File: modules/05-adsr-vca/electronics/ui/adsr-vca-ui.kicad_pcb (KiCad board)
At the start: 2 copper layers, 58 x 110 mm, 40 parts, among them J1 Conn_02x03_Odd_Even, J3 Conn_02x03_Odd_Even, J4 Conn_01x02, J5 Conn_01x06, J6 Conn_02x03_Odd_Even, J8 Conn_02x03_Odd_Even, Q1 2N3904, Q2 2N3906

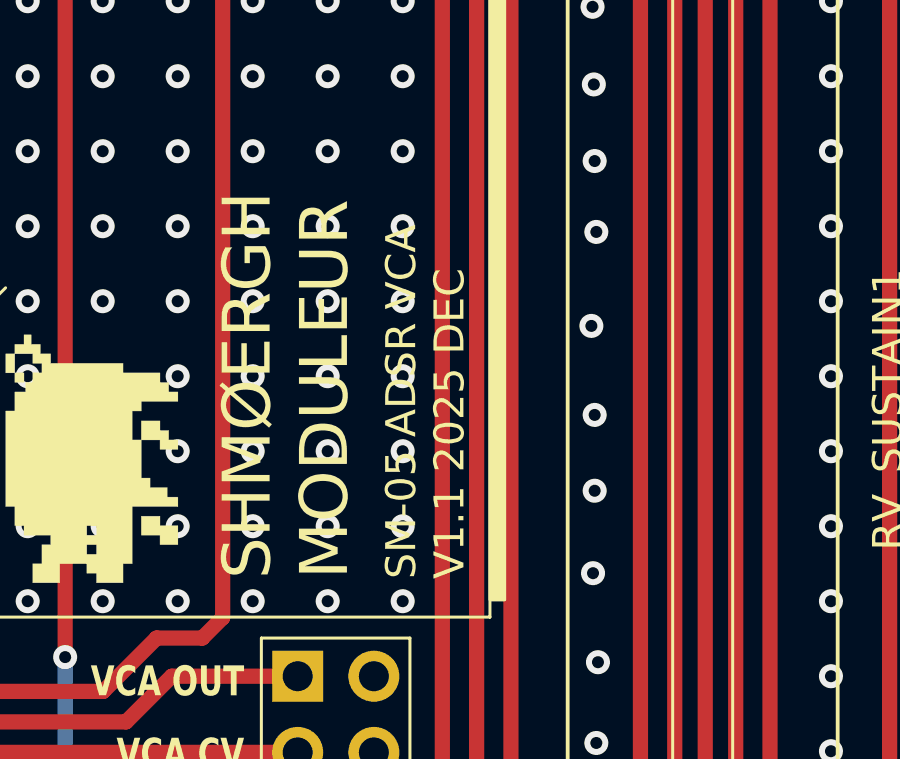
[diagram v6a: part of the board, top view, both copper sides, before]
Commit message: KiCAD version update - ADSR+VCA
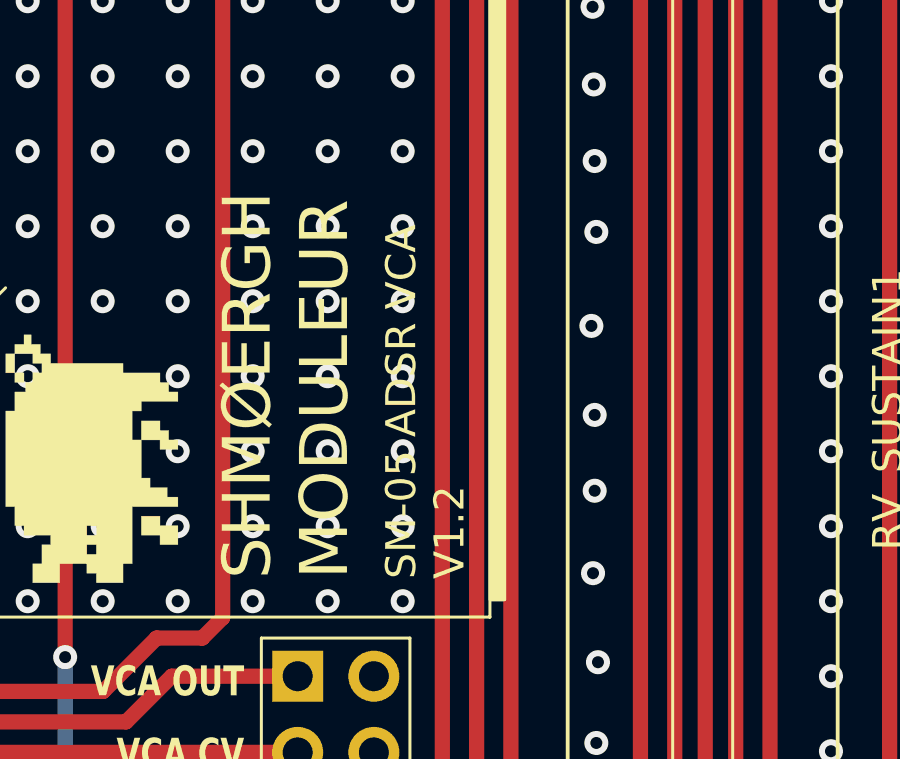
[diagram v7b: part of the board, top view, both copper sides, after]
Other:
- board text added: "SM-05 ADSR VCA V1.2"
- board text removed: "SM-05 ADSR VCA V1.1 2025 DEC"
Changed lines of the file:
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@@
 		)
 	)
-	(gr_text "SM-05 ADSR VCA\nV1.1 2025 DEC"
+	(gr_text "SM-05 ADSR VCA\nV1.2"
 		(at 161.1475 88.2595 90)
 		(layer "F.SilkS")
@@
 			(justify left bottom)
 		)
-		(render_cache "SM-05 ADSR VCA\nV1.1 2025 DEC" 90
+		(render_cache "SM-05 ADSR VCA\nV1.2" 90
 			(polygon
 				(pts
@@
 			(polygon
 				(pts
-					(xy 160.213874 85.207624) (xy 160.850249 85.207624) (xy 160.850249 85.462186) (xy 160.9775 85.462186)
-					(xy 160.9775 84.825811) (xy 160.850249 84.825811) (xy 160.850249 85.080374) (xy 159.959312 85.080374)
-					(xy 159.959312 85.207624) (xy 160.086624 85.207624) (xy 160.086624 85.462186) (xy 160.213874 85.462186)
-				)
-			)
-			(polygon
-				(pts
-					(xy 160.722998 83.682144) (xy 160.9775 83.682144) (xy 160.9775 83.04577) (xy 160.850249 83.04577)
-					(xy 160.850249 83.554894) (xy 160.722998 83.554894)
-				)
-			)
-			(polygon
-				(pts
-					(xy 160.086624 83.173081) (xy 159.959312 83.173081) (xy 159.959312 83.554894) (xy 160.086624 83.554894)
-				)
-			)
-			(polygon
-				(pts
-					(xy 160.086624 83.173081) (xy 160.341186 83.173081) (xy 160.341186 83.04577) (xy 160.086624 83.04577)
-				)
-			)
-			(polygon
-				(pts
-					(xy 160.595687 83.554894) (xy 160.722998 83.554894) (xy 160.722998 83.427582) (xy 160.595687 83.427582)
-				)
-			)
-			(polygon
-				(pts
-					(xy 160.086624 83.682144) (xy 160.213874 83.682144) (xy 160.213874 83.554894) (xy 160.086624 83.554894)
-				)
-			)
-			(polygon
-				(pts
-					(xy 160.341186 83.300332) (xy 160.468436 83.300332) (xy 160.468436 83.173081) (xy 160.341186 83.173081)
-				)
-			)
-			(polygon
-				(pts
-					(xy 160.468436 83.427582) (xy 160.595687 83.427582) (xy 160.595687 83.300332) (xy 160.468436 83.300332)
-				)
-			)
-			(polygon
-				(pts
-					(xy 160.086624 82.792123) (xy 160.850249 82.792123) (xy 160.850249 82.664873) (xy 160.595687 82.664873)
-					(xy 160.595687 82.537561) (xy 160.468436 82.537561) (xy 160.468436 82.664873) (xy 160.086624 82.664873)
-				)
-			)
-			(polygon
-				(pts
-					(xy 160.850249 82.664873) (xy 160.9775 82.664873) (xy 160.9775 82.28306) (xy 160.850249 82.28306)
-				)
-			)
-			(polygon
-				(pts
-					(xy 159.959312 82.664873) (xy 160.086624 82.664873) (xy 160.086624 82.28306) (xy 159.959312 82.28306)
-				)
-			)
-			(polygon
-				(pts
-					(xy 160.086624 82.28306) (xy 160.213874 82.28306) (xy 160.213874 82.410311) (xy 160.341186 82.410311)
-					(xy 160.341186 82.28306) (xy 160.850249 82.28306) (xy 160.850249 82.155749) (xy 160.086624 82.155749)
-				)
-			)
-			(polygon
-				(pts
-					(xy 160.341186 82.537561) (xy 160.468436 82.537561) (xy 160.468436 82.410311) (xy 160.341186 82.410311)
-				)
-			)
-			(polygon
-				(pts
-					(xy 160.722998 81.902102) (xy 160.9775 81.902102) (xy 160.9775 81.265728) (xy 160.850249 81.265728)
-					(xy 160.850249 81.774852) (xy 160.722998 81.774852)
-				)
-			)
-			(polygon
-				(pts
-					(xy 160.086624 81.393039) (xy 159.959312 81.393039) (xy 159.959312 81.774852) (xy 160.086624 81.774852)
-				)
-			)
-			(polygon
-				(pts
-					(xy 160.086624 81.393039) (xy 160.341186 81.393039) (xy 160.341186 81.265728) (xy 160.086624 81.265728)
-				)
-			)
-			(polygon
-				(pts
-					(xy 160.595687 81.774852) (xy 160.722998 81.774852) (xy 160.722998 81.64754) (xy 160.595687 81.64754)
-				)
-			)
-			(polygon
-				(pts
-					(xy 160.086624 81.902102) (xy 160.213874 81.902102) (xy 160.213874 81.774852) (xy 160.086624 81.774852)
-				)
-			)
-			(polygon
-				(pts
-					(xy 160.341186 81.52029) (xy 160.468436 81.52029) (xy 160.468436 81.393039) (xy 160.341186 81.393039)
-				)
-			)
-			(polygon
-				(pts
-					(xy 160.468436 81.64754) (xy 160.595687 81.64754) (xy 160.595687 81.52029) (xy 160.468436 81.52029)
-				)
-			)
-			(polygon
-				(pts
-					(xy 159.959312 81.012081) (xy 160.468436 81.012081) (xy 160.468436 80.503018) (xy 160.341186 80.503018)
-					(xy 160.341186 80.884831) (xy 160.086624 80.884831) (xy 160.086624 80.375707) (xy 159.959312 80.375707)
-				)
-			)
-			(polygon
-				(pts
-					(xy 160.468436 80.503018) (xy 160.850249 80.503018) (xy 160.850249 80.375707) (xy 160.468436 80.375707)
-				)
-			)
-			(polygon
-				(pts
-					(xy 160.850249 80.503018) (xy 160.850249 80.884831) (xy 160.9775 80.884831) (xy 160.9775 80.503018)
-				)
-			)
-			(polygon
-				(pts
-					(xy 160.850249 80.884831) (xy 160.722998 80.884831) (xy 160.722998 81.012081) (xy 160.850249 81.012081)
-				)
-			)
-			(polygon
-				(pts
-					(xy 159.959312 79.23204) (xy 160.9775 79.23204) (xy 160.9775 78.722976) (xy 160.850249 78.722976)
-					(xy 160.850249 79.104789) (xy 160.086624 79.104789) (xy 160.086624 78.722976) (xy 159.959312 78.722976)
-				)
-			)
-			(polygon
-				(pts
-					(xy 160.086624 78.722976) (xy 160.850249 78.722976) (xy 160.850249 78.595665) (xy 160.086624 78.595665)
-				)
-			)
-			(polygon
-				(pts
-					(xy 159.959312 78.342019) (xy 160.9775 78.342019) (xy 160.9775 77.705644) (xy 160.850249 77.705644)
-					(xy 160.850249 78.214768) (xy 160.468436 78.214768) (xy 160.468436 77.832956) (xy 160.341186 77.832956)
-					(xy 160.341186 78.214768) (xy 160.086624 78.214768) (xy 160.086624 77.705644) (xy 159.959312 77.705644)
-				)
-			)
-			(polygon
-				(pts
-					(xy 160.086624 77.451998) (xy 160.850249 77.451998) (xy 160.850249 77.324747) (xy 160.086624 77.324747)
-				)
-			)
-			(polygon
-				(pts
-					(xy 160.850249 77.324747) (xy 160.9775 77.324747) (xy 160.9775 76.942935) (xy 160.850249 76.942935)
-				)
-			)
-			(polygon
-				(pts
-					(xy 160.722998 76.942935) (xy 160.850249 76.942935) (xy 160.850249 76.815623) (xy 160.722998 76.815623)
-				)
-			)
-			(polygon
-				(pts
-					(xy 159.959312 77.324747) (xy 160.086624 77.324747) (xy 160.086624 76.942935) (xy 159.959312 76.942935)
-				)
-			)
-			(polygon
-				(pts
-					(xy 160.086624 76.942935) (xy 160.213874 76.942935) (xy 160.213874 76.815623) (xy 160.086624 76.815623)
-				)
-			)
+					(xy 160.722998 85.462186) (xy 160.9775 85.462186) (xy 160.9775 84.825811) (xy 160.850249 84.825811)
+					(xy 160.850249 85.334936) (xy 160.722998 85.334936)
+				)
+			)
+			(polygon
+				(pts
+					(xy 160.086624 84.953123) (xy 159.959312 84.953123) (xy 159.959312 85.334936) (xy 160.086624 85.334936)
+				)
+			)
+			(polygon
+				(pts
+					(xy 160.086624 84.953123) (xy 160.341186 84.953123) (xy 160.341186 84.825811) (xy 160.086624 84.825811)
+				)
+			)
+			(polygon
+				(pts
+					(xy 160.595687 85.334936) (xy 160.722998 85.334936) (xy 160.722998 85.207624) (xy 160.595687 85.207624)
+				)
+			)
+			(polygon
+				(pts
+					(xy 160.086624 85.462186) (xy 160.213874 85.462186) (xy 160.213874 85.334936) (xy 160.086624 85.334936)
+				)
+			)
+			(polygon
+				(pts
+					(xy 160.341186 85.080374) (xy 160.468436 85.080374) (xy 160.468436 84.953123) (xy 160.341186 84.953123)
+				)
+			)
+			(polygon
+				(pts
+					(xy 160.468436 85.207624) (xy 160.595687 85.207624) (xy 160.595687 85.080374) (xy 160.468436 85.080374)
+				)
+			)

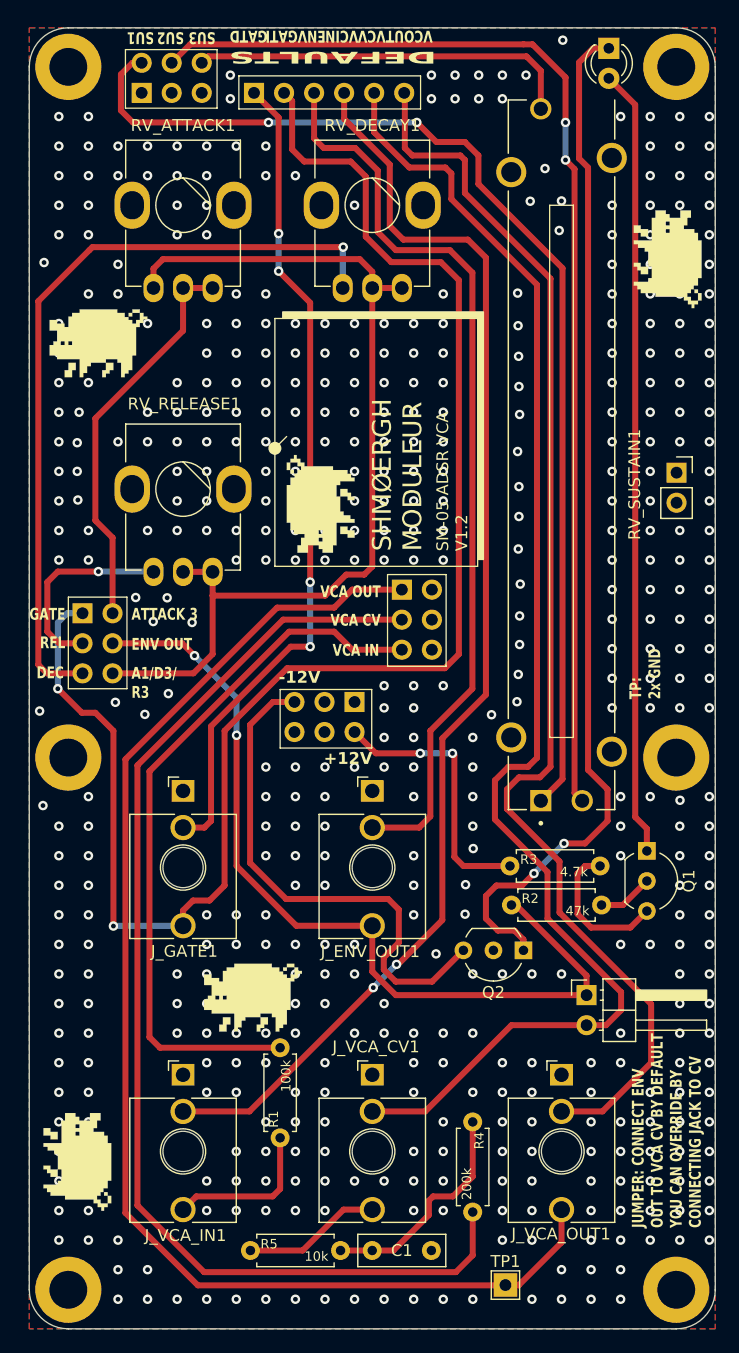
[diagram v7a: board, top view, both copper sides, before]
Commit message: Moduleur Hardware v1.1 update
PSU v1.1

- Replaced 1N4001 with 1N5822 Schottky diode for overall better performance (faster switch, less temperature dissipation, better surge behavior, ~0.2V voltage drop)
- Added 1.5KE36A TVS at DC jack for ESD protection

VCA v1.3

- Added test resistors to VCA output and VCA input

Brain v1.3

- Added testing resistor and protection diode to pulse output on UI board
- Updated Mounting Hole H3 to connect to GND so it's not necessary to use wired connection to ground the front and backpanel.
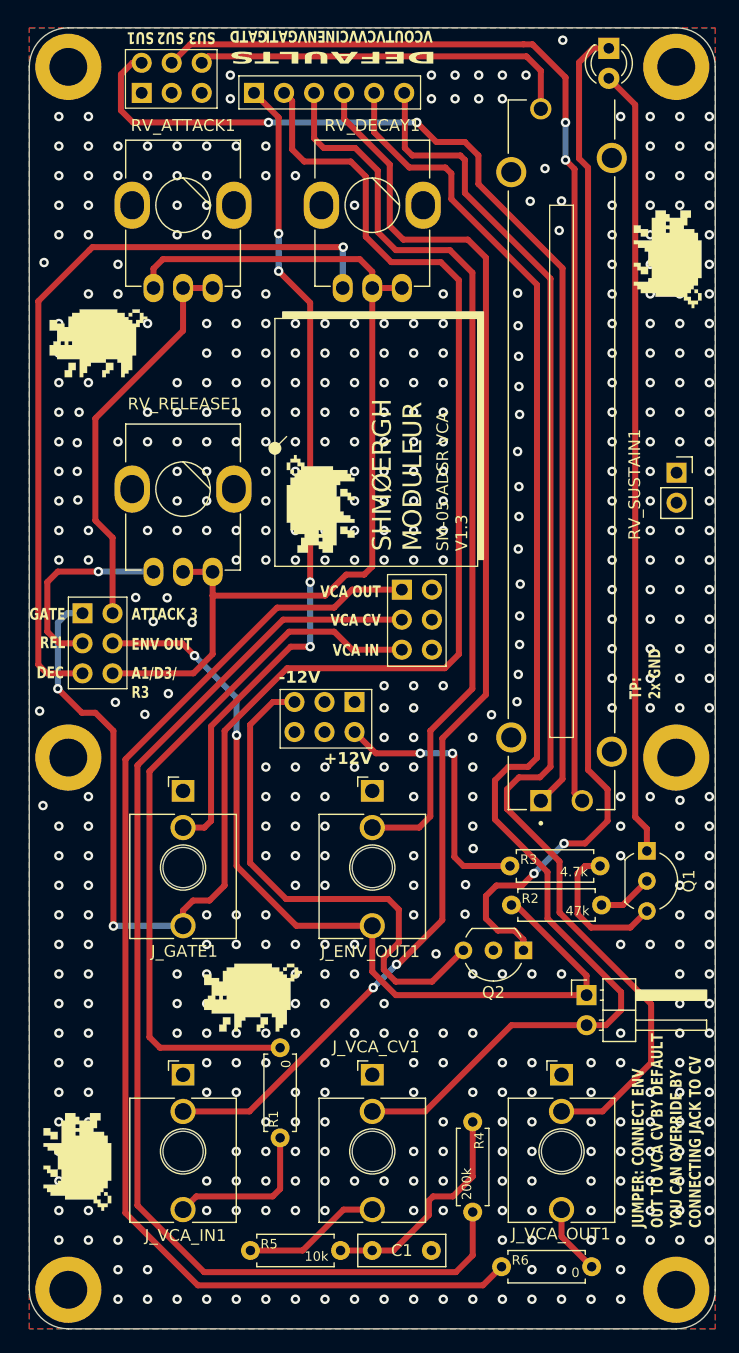
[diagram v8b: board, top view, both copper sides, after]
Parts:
- removed TP1: TestPoint, TestPoint:TestPoint_THTPad_2.0x2.0mm_Drill1.0mm
- added R6: 0, Shmoergh_Custom_Footprints:R_Axial_DIN0207_L6.3mm_D2.5mm_P7.62mm_Horizontal, F.Cu at (163.9, 148.7)
- R1: value 100k -> 0
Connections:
- J_VCA_OUT1 pad T: VCA_OUT -> Net-(J_VCA_OUT1-PadT)
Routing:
- net VCA_OUT: track 111.4 -> 102.7 mm
- net Net-(J_VCA_OUT1-PadT): track 0.00 -> 5.89 mm
- net GND: vias 500 -> 501
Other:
- board text added: "SM-05 ADSR VCA V1.3"
- board text removed: "SM-05 ADSR VCA V1.2"
